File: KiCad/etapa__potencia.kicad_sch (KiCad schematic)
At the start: 10 parts, among them K1 Fujitsu_FTR-LYAA005x, K2 Fujitsu_FTR-LYAA005x

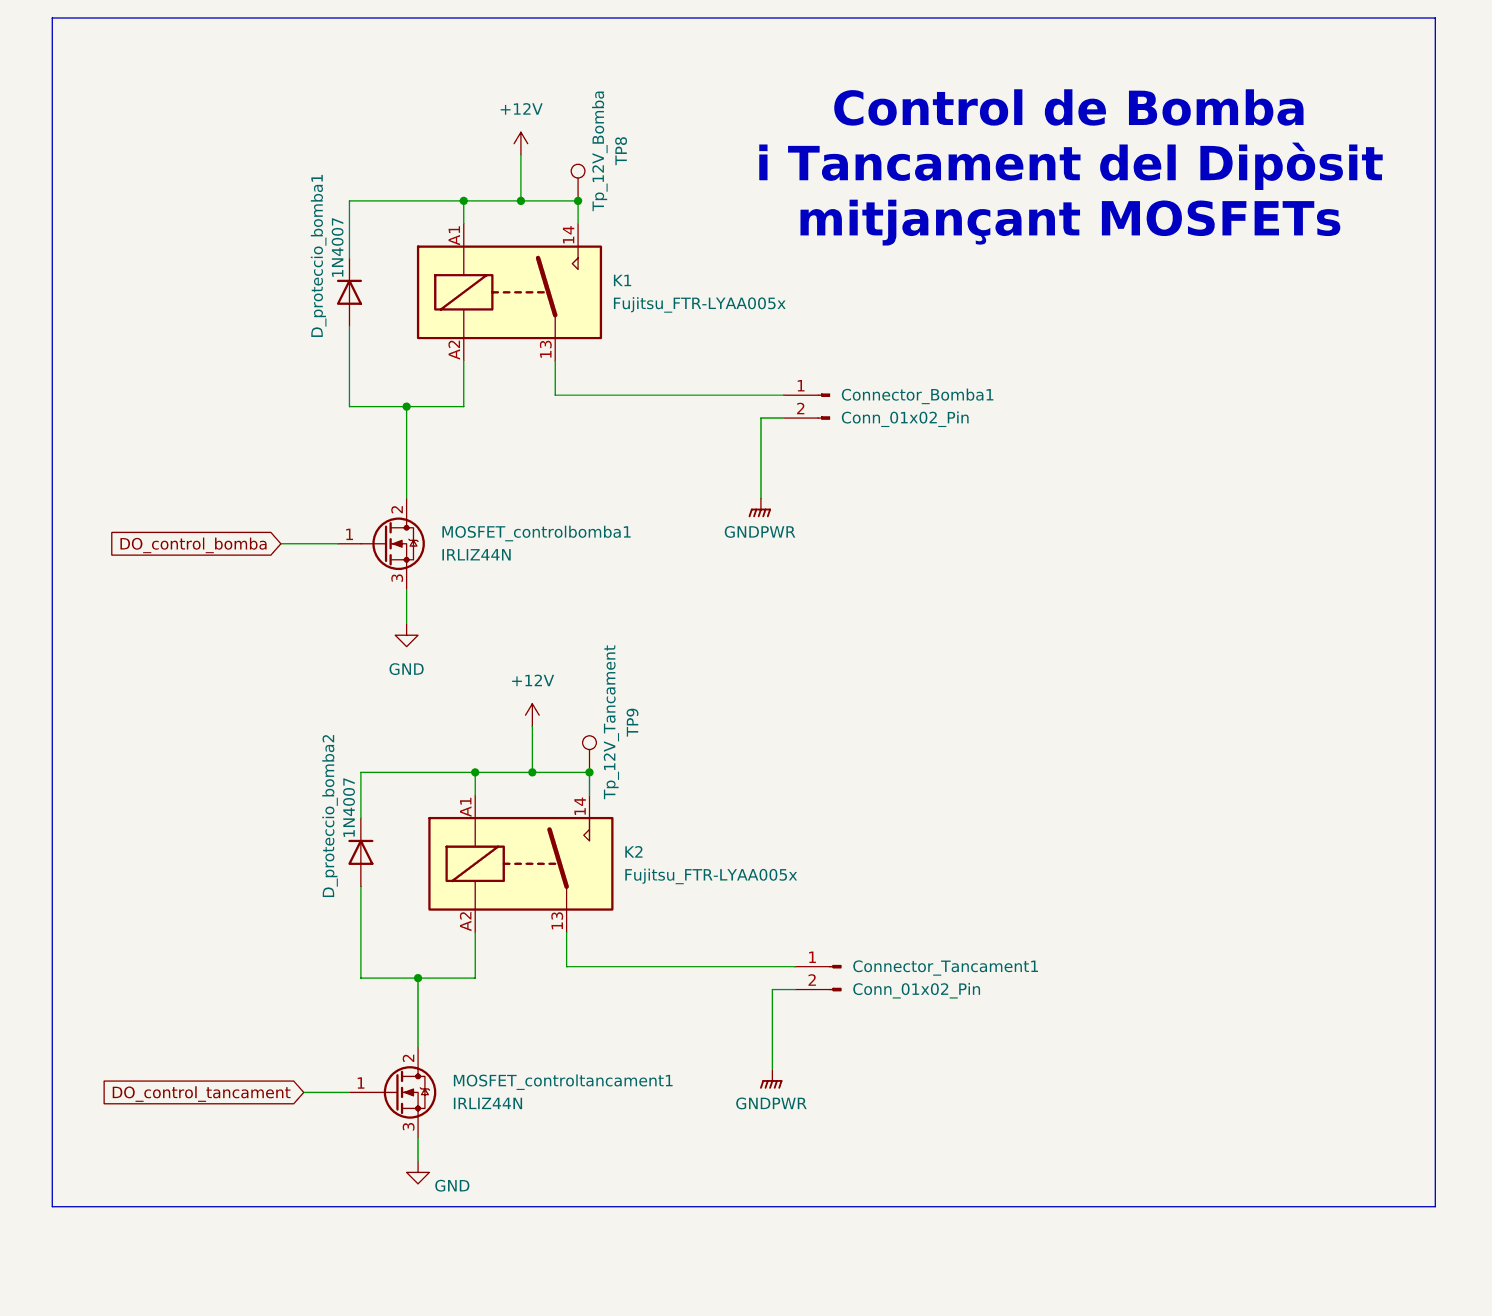
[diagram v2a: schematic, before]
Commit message: Algunes correccions del professor (esquemàtic i pcb)
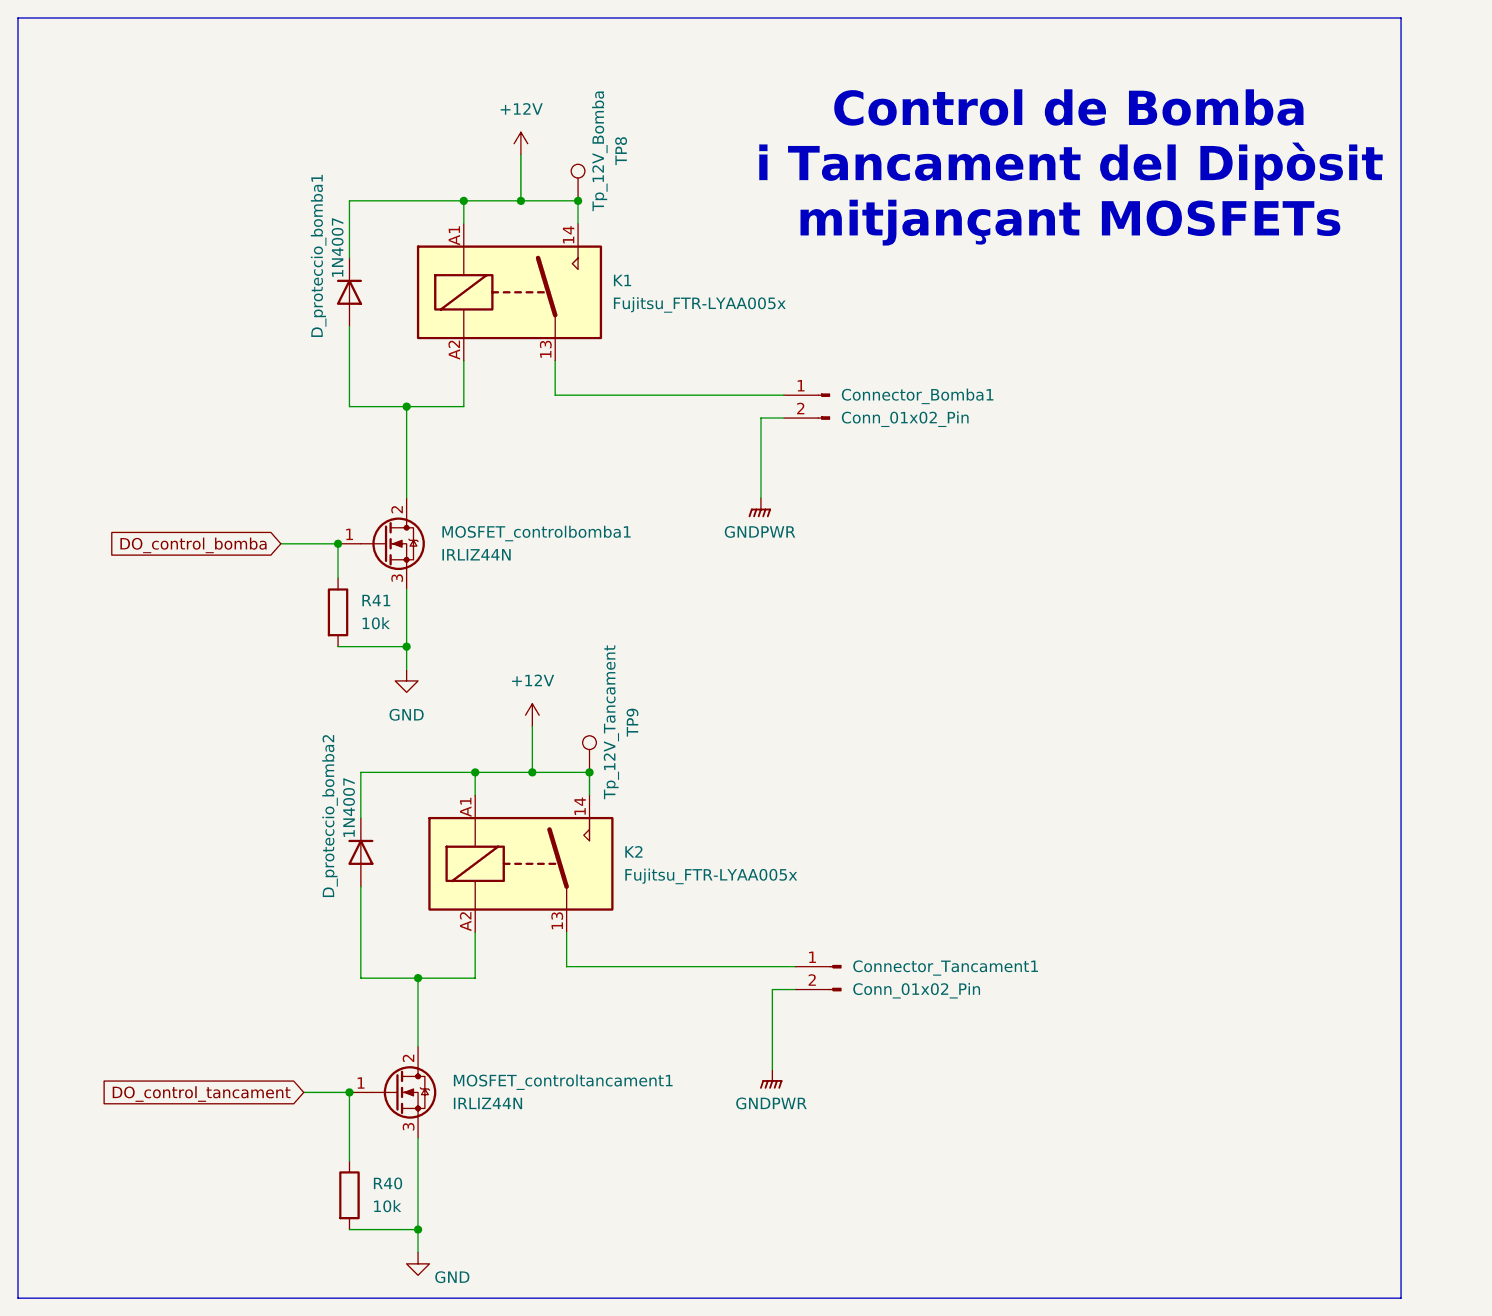
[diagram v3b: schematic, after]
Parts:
- added R40, R41: 10k, Resistor_SMD:R_0805_2012Metric, symbol Device:R
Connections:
- net DO_control_bomba: now also R41.1
- net DO_control_tancament: now also R40.1
- net GND: now also R40.2, R41.2
